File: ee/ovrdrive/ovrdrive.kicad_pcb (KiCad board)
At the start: 4 copper layers, 37.2 x 15 mm, 40 parts, among them J1 USB_A, Q1 Q_NMOS_DGS, U1 SM3257ENT, U2 FLASH, U3 ATtiny24A-MM, U4 74AUC1G32, U5 LMV321, U6 LM4040DBZ-2.5

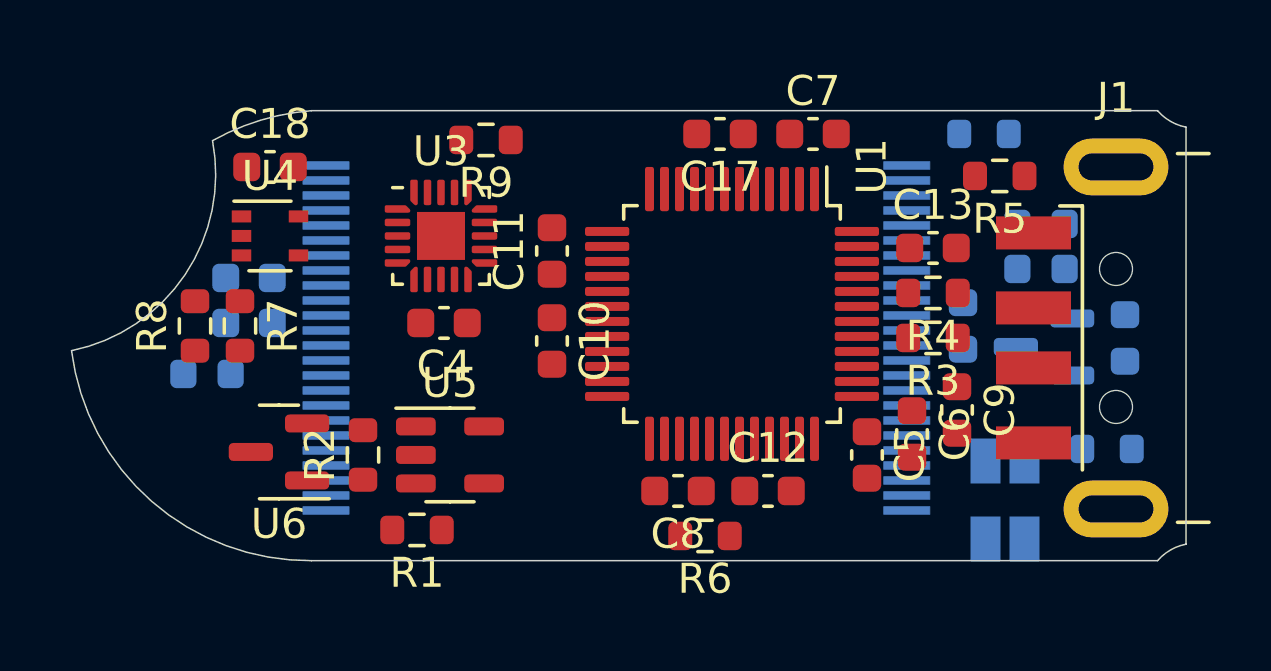
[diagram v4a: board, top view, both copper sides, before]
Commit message: Routed out the power.
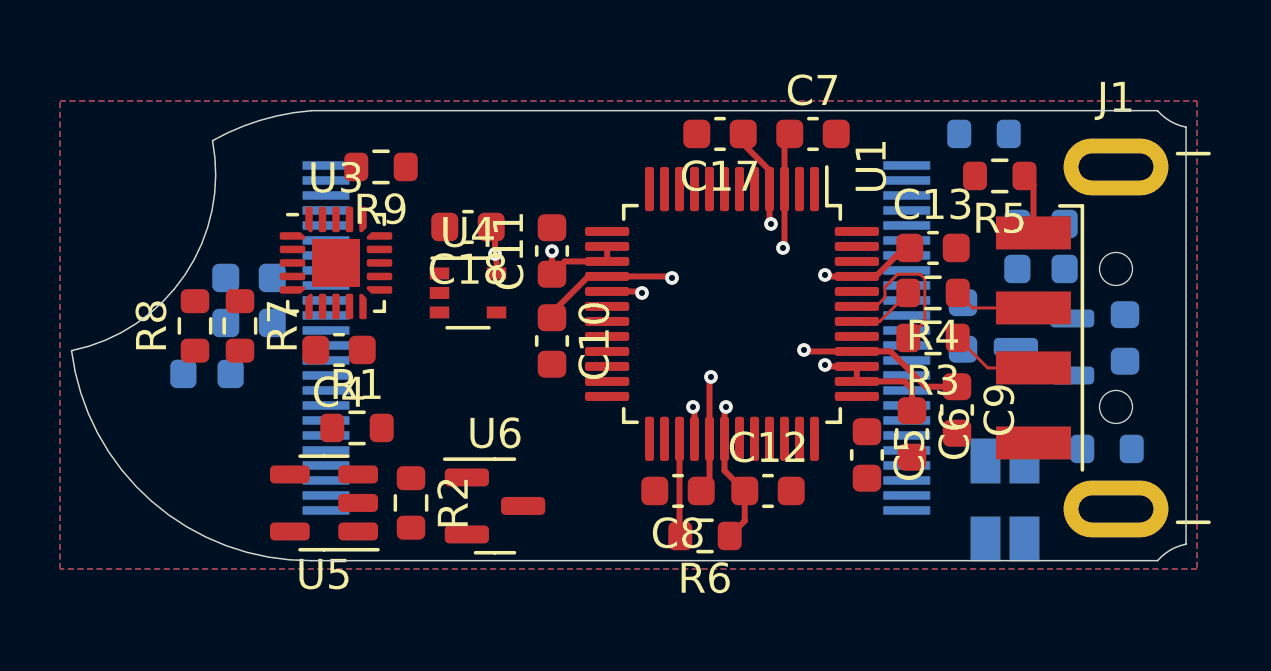
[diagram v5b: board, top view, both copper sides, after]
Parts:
- moved U6 7.42 mm to (121.4, 109.8), turned to 0 degrees
- moved C18 6.90 mm to (120.5, 100.5), turned to 180 degrees
- moved U4 6.87 mm to (120.5, 102.7)
- moved U5 4.49 mm to (115.7, 109.7), turned to 180 degrees
- moved R1 3.94 mm to (116.8, 107.2), turned to 0 degrees
- moved R9 3.61 mm to (117.6, 98.5)
- moved U3 3.61 mm to (116.1, 101.7)
- moved C4 3.61 mm to (116.2, 104.6)
- moved R2 2.26 mm to (118.6, 109.7), turned to -90 degrees
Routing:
- net +3.3V: track 0.00 -> 23.5 mm, vias 0 -> 8
- net +1V8: track 0.00 -> 18.1 mm, vias 0 -> 4
- net /DP: track 0.00 -> 5.18 mm
- net Net-(R6-Pad2): track 0.00 -> 3.25 mm
- net Net-(J1-Pad3): track 0.00 -> 2.94 mm
- net Net-(J1-Pad2): track 0.00 -> 2.73 mm
- net /DM: track 0.00 -> 2.11 mm
- net Net-(J1-Pad1): track 0.00 -> 2.02 mm
- added copper zone on In1.Cu, net +1V8
- added copper zone on In1.Cu, net +3.3V
- added copper zone on B.Cu, net GND
- added copper zone on F.Cu, net GND
- added copper zone on In1.Cu, net GND
- added copper zone on In2.Cu, net GND

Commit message: Working on the routing.
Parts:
- added C15: 100nF, Capacitor_SMD:C_0603_1608Metric, F.Cu at (112.9, 109.4)
- added J3: AVR-ISP-6, Connector_PinHeader_2.54mm:PinHeader_2x03_P2.54mm_Vertical_SMD, F.Cu at (123.3, 57.6)
- JP1, JP2, R10: moved to F.Cu
- moved JP1 5.73 mm to (133.2, 110.7)
- moved R10 3.26 mm to (134.6, 98.4), turned to -90 degrees
- moved JP2 2.26 mm to (136.2, 110.4)
- moved C4 1.42 mm to (115.3, 105.7)
- moved R7 1.42 mm to (112.0, 104.9)
- moved R8 1.42 mm to (110.5, 104.9)
- moved R9 1.42 mm to (116.7, 99.6)
- moved U3 1.42 mm to (115.2, 102.8)
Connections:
- net Net-(U1-Pad10) renamed /FD7
- net Net-(U1-Pad11) renamed /FD6
- net Net-(U1-Pad12) renamed /FD5
- net Net-(U1-Pad13) renamed /FD4
- net Net-(U1-Pad18) renamed /FD3
- net Net-(U1-Pad19) renamed /FD2
- net Net-(U1-Pad20) renamed /FD1
- net Net-(U1-Pad21) renamed /FD0
- U2 pad 10: unconnected-(U2-Pad10) -> /~{CE1}
- U2 pad 14: unconnected-(U2-Pad14) -> /~{CE2}
- U2 pad 15: unconnected-(U2-Pad15) -> /~{CE3}
- U2 pad 35: unconnected-(U2-Pad35) -> /DQS
- U2 pad 4: unconnected-(U2-Pad4) -> /RB0
- U2 pad 5: unconnected-(U2-Pad5) -> /RB1
- U2 pad 6: unconnected-(U2-Pad6) -> /RB0
- U2 pad 7: unconnected-(U2-Pad7) -> /RB1
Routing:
- net +5V: track 0.00 -> 36.7 mm, vias 0 -> 3
- net /Vs: track 0.00 -> 6.73 mm
- net Net-(JP2-Pad2): track 0.00 -> 6.72 mm
- net Net-(JP1-Pad2): track 0.00 -> 5.93 mm
- net Net-(R1-Pad2): track 0.00 -> 4.05 mm
- net Net-(J2-Pad2): track 0.00 -> 1.81 mm
- net GND: vias 0 -> 2

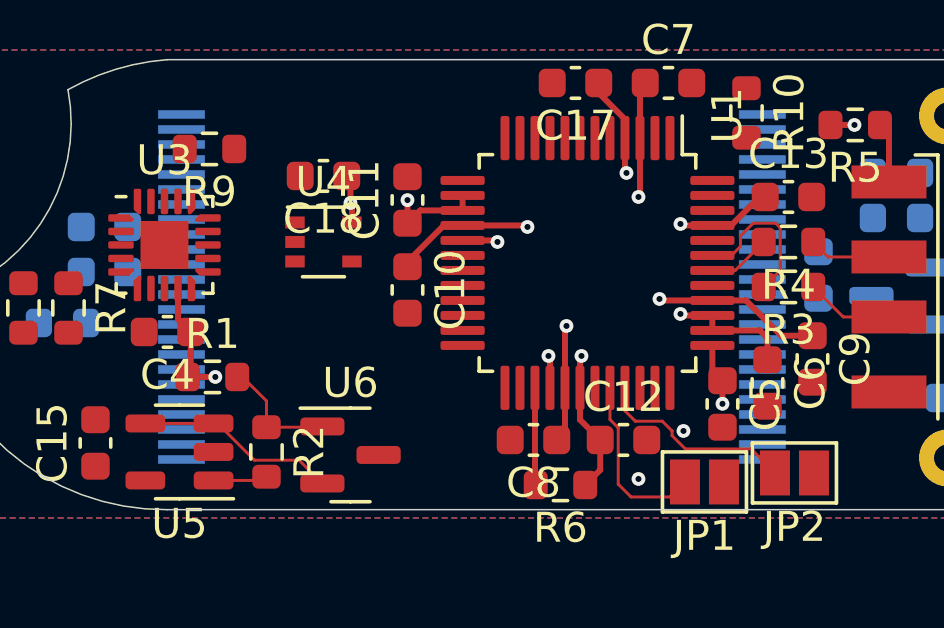
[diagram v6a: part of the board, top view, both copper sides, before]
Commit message: Routed out the datalines.
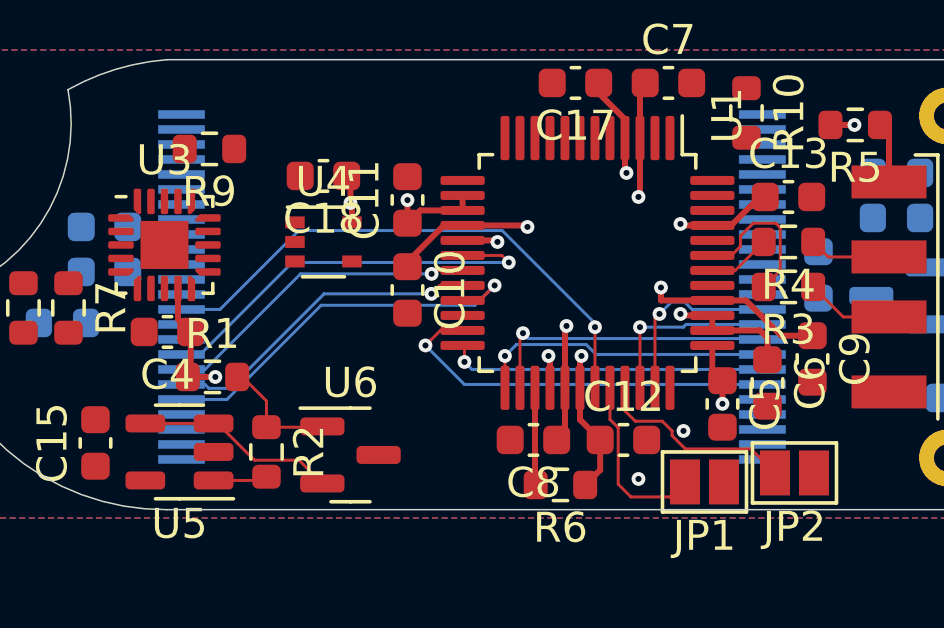
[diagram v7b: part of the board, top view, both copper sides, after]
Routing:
- net /DQS: track 0.00 -> 18.3 mm, vias 0 -> 1
- net /FD3: track 0.00 -> 13.8 mm, vias 0 -> 1
- net /FD0: track 0.00 -> 13.3 mm, vias 0 -> 1
- net /~{WP}: track 0.00 -> 13.2 mm, vias 0 -> 1
- net /FD1: track 0.00 -> 10.8 mm, vias 0 -> 1
- net /FD2: track 0.00 -> 10.7 mm, vias 0 -> 1
- net /~{WE}: track 0.00 -> 10.6 mm, vias 0 -> 1
- net /ALE: track 0.00 -> 9.93 mm, vias 0 -> 1
- net /CLE: track 0.00 -> 9.93 mm, vias 0 -> 1
- net /~{CE2}: track 0.00 -> 6.22 mm, vias 0 -> 1
- net /~{CE3}: track 0.00 -> 6.14 mm, vias 0 -> 1
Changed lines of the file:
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@@
   (gr_line (start 144.434463 97.173719) (end 144.434463 111.073719) (layer "Edge.Cuts") (width 0.05))
   (gr_line (start 115.284463 96.623719) (end 143.484463 96.623719) (layer "Edge.Cuts") (width 0.05))
+  (segment (start 131.75 104.65) (end 131.75 104.22) (width 0.2) (layer "F.Cu") (net 2))
   (segment (start 133.4625 104.65) (end 134.584315 104.65) (width 0.2) (layer "F.Cu") (net 2))
   (segment (start 128.55 105.55) (end 128.6 105.5) (width 0.2) (layer "F.Cu") (net 2))
-  (segment (start 131.75 104.65) (end 131.7 104.6) (width 0.2) (layer "F.Cu") (net 2))
   (segment (start 125.1375 102.15) (end 127.25 102.15) (width 0.2) (layer "F.Cu") (net 2))
   (segment (start 123.3 103.525) (end 123.3 103.361091) (width 0.2) (layer "F.Cu") (net 2))
@@
   (segment (start 131.05 97.575) (end 131.05 99.2375) (width 0.2) (layer "F.Cu") (net 2))
   (segment (start 128.55 107.5625) (end 128.55 105.55) (width 0.2) (layer "F.Cu") (net 2))
+  (via (at 131.75 104.22) (size 0.46) (drill 0.2) (layers "F.Cu" "B.Cu") (net 2))
   (via (at 127.3 102.2) (size 0.46) (drill 0.2) (layers "F.Cu" "B.Cu") (net 2))
   (via (at 128.6 105.5) (size 0.46) (drill 0.2) (layers "F.Cu" "B.Cu") (net 2))
-  (via (at 131.7 104.6) (size 0.46) (drill 0.2) (layers "F.Cu" "B.Cu") (net 2))
   (via (at 131 101.2) (size 0.46) (drill 0.2) (layers "F.Cu" "B.Cu") (net 2))
   (segment (start 137.825 105.2) (end 136.825 104.2) (width 0.1) (layer "F.Cu") (net 3))
@@
   (segment (start 127.55 110.775) (end 127.575 110.8) (width 0.2) (layer "F.Cu") (net 16))
   (segment (start 127.55 107.5625) (end 127.55 110.775) (width 0.2) (layer "F.Cu") (net 16))
+  (segment (start 129.55 107.5625) (end 129.55 105.5405) (width 0.1) (layer "F.Cu") (net 23))
+  (via (at 129.55 105.5405) (size 0.46) (drill 0.2) (layers "F.Cu" "B.Cu") (net 23))
+  (segment (start 129.55 105.412598) (end 126.457402 102.32) (width 0.1) (layer "B.Cu") (net 23))
+  (segment (start 129.55 105.5405) (end 129.55 105.412598) (width 0.1) (layer "B.Cu") (net 23))
+  (segment (start 119.68 102.32) (end 117.05 104.95) (width 0.1) (layer "B.Cu") (net 23))
+  (segment (start 126.457402 102.32) (end 119.68 102.32) (width 0.1) (layer "B.Cu") (net 23))
+  (segment (start 117.05 104.95) (end 115.7675 104.95) (width 0.1) (layer "B.Cu") (net 23))
+  (segment (start 131.05 107.5625) (end 131.05 105.5405) (width 0.1) (layer "F.Cu") (net 47))
+  (via (at 131.05 105.5405) (size 0.46) (drill 0.2) (layers "F.Cu" "B.Cu") (net 47))
+  (segment (start 132.496902 105.5405) (end 131.05 105.5405) (width 0.1) (layer "B.Cu") (net 47))
+  (segment (start 132.587402 105.45) (end 132.496902 105.5405) (width 0.1) (layer "B.Cu") (net 47))
+  (segment (start 135.1275 105.45) (end 132.587402 105.45) (width 0.1) (layer "B.Cu") (net 47))
+  (segment (start 131.7 105.1) (end 131.55 105.25) (width 0.1) (layer "F.Cu") (net 48))
+  (segment (start 131.55 105.25) (end 131.55 107.5625) (width 0.1) (layer "F.Cu") (net 48))
+  (via (at 131.7 105.1) (size 0.46) (drill 0.2) (layers "F.Cu" "B.Cu") (net 48))
+  (segment (start 135.1275 104.95) (end 132.787402 104.95) (width 0.1) (layer "B.Cu") (net 48))
+  (segment (start 132.537402 104.7) (end 132.1 104.7) (width 0.1) (layer "B.Cu") (net 48))
+  (segment (start 132.787402 104.95) (end 132.537402 104.7) (width 0.1) (layer "B.Cu") (net 48))
+  (segment (start 132.1 104.7) (end 131.7 105.1) (width 0.1) (layer "B.Cu") (net 48))
+  (segment (start 124.4 105.65) (end 125.1375 105.65) (width 0.1) (layer "F.Cu") (net 51))
+  (segment (start 123.9 106.15) (end 124.4 105.65) (width 0.1) (layer "F.Cu") (net 51))
+  (via (at 123.9 106.15) (size 0.46) (drill 0.2) (layers "F.Cu" "B.Cu") (net 51))
+  (segment (start 135.1275 107.45) (end 125.2 107.45) (width 0.1) (layer "B.Cu") (net 51))
+  (segment (start 125.2 107.45) (end 123.9 106.15) (width 0.1) (layer "B.Cu") (net 51))
+  (segment (start 125.2 106.2125) (end 125.1375 106.15) (width 0.1) (layer "F.Cu") (net 52))
+  (segment (start 125.2 106.7) (end 125.2 106.2125) (width 0.1) (layer "F.Cu") (net 52))
+  (via (at 125.2 106.7) (size 0.46) (drill 0.2) (layers "F.Cu" "B.Cu") (net 52))
+  (segment (start 125.45 106.95) (end 125.2 106.7) (width 0.1) (layer "B.Cu") (net 52))
+  (segment (start 135.1275 106.95) (end 125.45 106.95) (width 0.1) (layer "B.Cu") (net 52))
+  (segment (start 126.55 106.5) (end 126.55 107.5625) (width 0.1) (layer "F.Cu") (net 53))
+  (via (at 126.55 106.5) (size 0.46) (drill 0.2) (layers "F.Cu" "B.Cu") (net 53))
+  (segment (start 129.587402 106.45) (end 129.257402 106.12) (width 0.1) (layer "B.Cu") (net 53))
+  (segment (start 126.93 106.12) (end 126.55 106.5) (width 0.1) (layer "B.Cu") (net 53))
+  (segment (start 129.257402 106.12) (end 126.93 106.12) (width 0.1) (layer "B.Cu") (net 53))
+  (segment (start 135.1275 106.45) (end 129.587402 106.45) (width 0.1) (layer "B.Cu") (net 53))
+  (segment (start 127.05 105.8405) (end 127.15 105.7405) (width 0.1) (layer "F.Cu") (net 54))
+  (segment (start 127.05 107.5625) (end 127.05 105.8405) (width 0.1) (layer "F.Cu") (net 54))
+  (via (at 127.15 105.7405) (size 0.46) (drill 0.2) (layers "F.Cu" "B.Cu") (net 54))
+  (segment (start 127.3295 105.92) (end 127.15 105.7405) (width 0.1) (layer "B.Cu") (net 54))
+  (segment (start 135.1275 105.95) (end 135.0975 105.92) (width 0.1) (layer "B.Cu") (net 54))
+  (segment (start 135.0975 105.92) (end 127.3295 105.92) (width 0.1) (layer "B.Cu") (net 54))
   (segment (start 116.974264 108.75) (end 118.199264 109.975) (width 0.1) (layer "F.Cu") (net 55))
   (segment (start 119.6875 109.975) (end 120.4625 110.75) (width 0.1) (layer "F.Cu") (net 55))
@@
   (segment (start 135.7045 108.0955) (end 133.8 108.0955) (width 0.2) (layer "In1.Cu") (net 60))
   (segment (start 136.6 100) (end 136.3 100.3) (width 0.2) (layer "In1.Cu") (net 60))
+  (segment (start 126.442727 103.15) (end 126.677375 103.384648) (width 0.1) (layer "F.Cu") (net 79))
+  (segment (start 125.1375 103.15) (end 126.442727 103.15) (width 0.1) (layer "F.Cu") (net 79))
+  (via (at 126.677375 103.384648) (size 0.46) (drill 0.2) (layers "F.Cu" "B.Cu") (net 79))
+  (segment (start 119.458423 103.384648) (end 126.677375 103.384648) (width 0.1) (layer "B.Cu") (net 79))
+  (segment (start 115.7675 106.45) (end 116.393071 106.45) (width 0.1) (layer "B.Cu") (net 79))
+  (segment (start 116.393071 106.45) (end 119.458423 103.384648) (width 0.1) (layer "B.Cu") (net 79))
+  (segment (start 125.1375 103.65) (end 124.218648 103.65) (width 0.1) (layer "F.Cu") (net 80))
+  (segment (start 124.218648 103.65) (end 124.1045 103.764148) (width 0.1) (layer "F.Cu") (net 80))
+  (via (at 124.1045 103.764148) (size 0.46) (drill 0.2) (layers "F.Cu" "B.Cu") (net 80))
+  (segment (start 116.55 106.95) (end 115.7675 106.95) (width 0.1) (layer "B.Cu") (net 80))
+  (segment (start 124.1045 103.764148) (end 119.735852 103.764148) (width 0.1) (layer "B.Cu") (net 80))
+  (segment (start 119.735852 103.764148) (end 116.55 106.95) (width 0.1) (layer "B.Cu") (net 80))
+  (segment (start 124.377254 104.15) (end 124.097461 104.429793) (width 0.1) (layer "F.Cu") (net 81))
+  (segment (start 125.1375 104.15) (end 124.377254 104.15) (width 0.1) (layer "F.Cu") (net 81))
+  (via (at 124.097461 104.429793) (size 0.46) (drill 0.2) (layers "F.Cu" "B.Cu") (net 81))
+  (segment (start 120.520207 104.429793) (end 117.37 107.58) (width 0.1) (layer "B.Cu") (net 81))
+  (segment (start 124.097461 104.429793) (end 120.520207 104.429793) (width 0.1) (layer "B.Cu") (net 81))
+  (segment (start 117.37 107.58) (end 116.68 107.58) (width 0.1) (layer "B.Cu") (net 81))
+  (segment (start 116.55 107.45) (end 115.7675 107.45) (width 0.1) (layer "B.Cu") (net 81))
+  (segment (start 116.68 107.58) (end 116.55 107.45) (width 0.1) (layer "B.Cu") (net 81))
+  (segment (start 125.7045 104.65) (end 126.2045 104.15) (width 0.1) (layer "F.Cu") (net 82))
+  (segment (start 125.1375 104.65) (end 125.7045 104.65) (width 0.1) (layer "F.Cu") (net 82))
+  (via (at 126.2045 104.15) (size 0.46) (drill 0.2) (layers "F.Cu" "B.Cu") (net 82))
+  (segment (start 117.282842 107.95) (end 115.7675 107.95) (width 0.1) (layer "B.Cu") (net 82))
+  (segment (start 125.544707 104.809793) (end 120.423049 104.809793) (width 0.1) (layer "B.Cu") (net 82))
+  (segment (start 120.423049 104.809793) (end 117.282842 107.95) (width 0.1) (layer "B.Cu") (net 82))
+  (segment (start 126.2045 104.15) (end 125.544707 104.809793) (width 0.1) (layer "B.Cu") (net 82))
   (zone (net 59) (net_name "GND") (layers "F.Cu" "In1.Cu" "In2.Cu" "B.Cu") (hatch edge 0.508)
     (connect_pads yes (clearance 0.1))

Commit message: Initial routing complete.
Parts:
- removed J3: AVR-ISP-6, Connector_PinHeader_2.54mm:PinHeader_2x03_P2.54mm_Vertical_SMD
- added TP1: TestPoint, TestPoint:TestPoint_Pad_1.0x1.0mm, F.Cu at (121.0, 106.9)
- added TP2: TestPoint, TestPoint:TestPoint_Pad_1.0x1.0mm, F.Cu at (113.5, 99.6)
- added TP3: TestPoint, TestPoint:TestPoint_Pad_1.0x1.0mm, F.Cu at (115.7, 99.6)
- added TP4: TestPoint, TestPoint:TestPoint_Pad_1.0x1.0mm, F.Cu at (112.0, 103.1)
- added TP5: TestPoint, TestPoint:TestPoint_Pad_1.0x1.0mm, F.Cu at (118.4, 105.2)
- added TP6: TestPoint, TestPoint:TestPoint_Pad_1.0x1.0mm, F.Cu at (125.0, 109.3)
- D1: moved to F.Cu
- moved C1 23.8 mm to (136.9, 104.3), turned to -90 degrees
- moved D1 7.59 mm to (118.2, 101.2), turned to -90 degrees
- moved C3 2.61 mm to (137.2, 101.2)
- moved R11 2.17 mm to (139.8, 107.0), turned to 0 degrees
- moved R9 1.59 mm to (117.5, 98.2), turned to -90 degrees
- moved R8 1.19 mm to (110.8, 106.0), turned to -90 degrees
- moved R7 0.85 mm to (112.3, 105.7), turned to 90 degrees
- moved C2 0.78 mm to (113.9, 104.0), turned to -90 degrees
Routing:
- net /Distruct_PWM: track 0.00 -> 41.4 mm, vias 0 -> 2
- net /KILL: track 0.00 -> 40.6 mm, vias 0 -> 1
- net +3.3V: track 23.5 -> 40.1 mm
- net Net-(U2-Pad9): track 0.00 -> 15.0 mm, vias 0 -> 1
- net /FD7: track 0.00 -> 13.8 mm, vias 0 -> 1
- net /INHIBIT: track 0.00 -> 13.8 mm, vias 0 -> 2
- net /FD6: track 0.00 -> 13.2 mm, vias 0 -> 1
- net /FD5: track 0.00 -> 12.1 mm, vias 0 -> 1
- net /~{CE}: track 0.00 -> 11.9 mm, vias 0 -> 2
- net +5V: track 36.7 -> 47.9 mm, vias 3 -> 5
- net /FD4: track 0.00 -> 10.5 mm, vias 0 -> 1
- net /RB0: track 0.00 -> 9.40 mm, vias 0 -> 1
- net /~{CE1}: track 0.00 -> 9.18 mm, vias 0 -> 1
- net /~{RE}: track 0.00 -> 7.76 mm, vias 0 -> 1
- net /RB1: track 0.00 -> 7.38 mm, vias 0 -> 1
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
